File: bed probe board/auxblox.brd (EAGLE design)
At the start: 20 x 10.1 mm, 4 parts, among them CN1 3p-2.54, CN2 3p-2.54

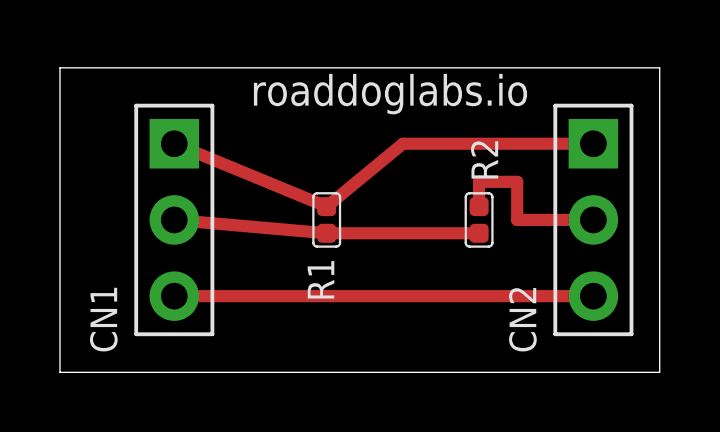
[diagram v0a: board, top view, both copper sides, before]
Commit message: update bed probe board
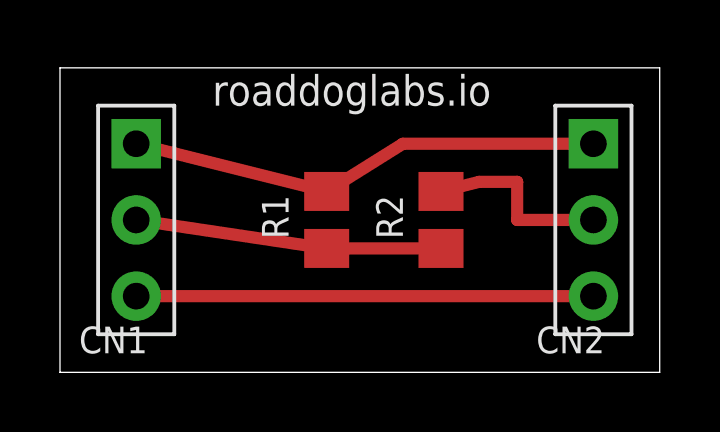
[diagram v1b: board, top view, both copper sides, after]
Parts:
- R1: value 910K 1/16W -> 1k; device Seeed-Resistor-2016:R0402 -> resistor:R0805
- R2: device Seeed-Resistor-2016:R0402 -> resistor:R0805
- moved CN1 1.27 mm to (16.5, 40.6)
- moved R2 1.27 mm to (26.7, 40.6), turned to 90 degrees
- turned R1 to 270 degrees
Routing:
- net N$1: track 14.0 -> 15.2 mm
- net N$4: track 15.1 -> 15.9 mm
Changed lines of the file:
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@@
 <?xml version="1.0" encoding="utf-8"?>
 <!DOCTYPE eagle SYSTEM "eagle.dtd">
-<eagle version="7.5.0">
+<eagle version="7.6.0">
 <drawing>
 <settings>
@@
 <wire x1="33.96" y1="45.71" x2="13.97" y2="45.71" width="0" layer="20"/>
 <wire x1="13.97" y1="45.71" x2="13.97" y2="35.56" width="0" layer="20"/>
-<text x="20.32" y="44.45" size="1.016" layer="21">roaddoglabs.io</text>
+<text x="19.05" y="44.45" size="1.016" layer="21">roaddoglabs.io</text>
 </plain>
 <attributes>
@@
 </class>
 </classes>
-<designrules name="SeeedStudio_2layer_DRU_no_angle_20140221">
-<description language="de">&lt;b&gt;EAGLE Design Rules&lt;/b&gt;
-&lt;p&gt;
-Die Standard-Design-Rules sind so gewählt, dass sie für
-die meisten Anwendungen passen. Sollte ihre Platine
-besondere Anforderungen haben, treffen Sie die erforderlichen
-Einstellungen hier und speichern die Design Rules unter
-einem neuen Namen ab.</description>
-<description language="en">&lt;b&gt;EAGLE Design Rules&lt;/b&gt;
-&lt;p&gt;
-The default Design Rules have been set to cover
-a wide range of applications. Your particular design
-may have different requirements, so please make the
-necessary adjustments and save your customized
-design rules under a new name.</description>
-<description language="zh">&lt;b&gt;Seeed Studio EAGLE Design Rules&lt;/b&gt;
-</description>
+<designrules name="dirt_cheap_dirty_boards.v1">
+<description language="en">&lt;b&gt;Dirty Cheap Dirty Board Design Rules&lt;/b&gt;
+&lt;br&gt;
+&lt;br&gt;Min width/Spacing: 5/5mil
+&lt;br&gt;Min diameter of finished hole 12mil</description>
 <param name="layerSetup" value="(1*16)"/>
 <param name="mtCopper" value="0.035mm 0.0175mm 0.035mm 0.035mm 0.035mm 0.035mm 0.035mm 0.035mm 0.035mm 0.035mm 0.035mm 0.035mm 0.035mm 0.035mm 0.0175mm 0.035mm"/>
 <param name="mtIsolate" value="1.5mm 1.1mm 0.2mm 0.15mm 0.2mm 0.15mm 0.2mm 0.15mm 0.2mm 0.15mm 0.2mm 0.15mm 0.2mm 0.15mm 0.2mm"/>
-<param name="mdWireWire" value="6mil"/>
-<param name="mdWirePad" value="6mil"/>
-<param name="mdWireVia" value="6mil"/>
-<param name="mdPadPad" value="6mil"/>
-<param name="mdPadVia" value="6mil"/>
-<param name="mdViaVia" value="6mil"/>
+<param name="mdWireWire" value="5mil"/>
+<param name="mdWirePad" value="5mil"/>
+<param name="mdWireVia" value="5mil"/>
+<param name="mdPadPad" value="5mil"/>
+<param name="mdPadVia" value="5mil"/>
+<param name="mdViaVia" value="5mil"/>
 <param name="mdSmdPad" value="0mil"/>
 <param name="mdSmdVia" value="0mil"/>
@@
 <param name="mdDrill" value="10mil"/>
 <param name="mdSmdStop" value="0mil"/>
-<param name="msWidth" value="6mil"/>
+<param name="msWidth" value="5mil"/>
 <param name="msDrill" value="12mil"/>
 <param name="msMicroVia" value="12mil"/>
@@
 <param name="mlMinCreamFrame" value="0mil"/>
 <param name="mlMaxCreamFrame" value="0mil"/>
-<param name="mlViaStopLimit" value="100mil"/>
+<param name="mlViaStopLimit" value="25mil"/>
 <param name="srRoundness" value="0"/>
 <param name="srMinRoundness" value="0mil"/>
@@
 </autorouter>
 <elements>
-<element name="R1" library="Seeed-Resistor-2016" package="R0402" value="910K 1/16W" x="22.86" y="40.64" smashed="yes">
-<attribute name="MPN" value="RC0402JR-07910KR" x="22.86" y="40.64" size="1.778" layer="27" display="off"/>
-<attribute name="NAME" x="22.225" y="39.37" size="0.889" layer="25" ratio="11" rot="R270"/>
+<element name="R1" library="resistor" package="R0805" value="1k" x="22.86" y="40.64" smashed="yes" rot="R270">
+<attribute name="NAME" x="21.59" y="40.005" size="0.889" layer="25" ratio="11" rot="R90"/>
 </element>
-<element name="R2" library="Seeed-Resistor-2016" package="R0402" value="3.3K" x="27.94" y="40.64" smashed="yes" rot="R180">
-<attribute name="MPN" value="RC0402JR-073K3L" x="27.94" y="40.64" size="1.778" layer="27" rot="R180" display="off"/>
-<attribute name="NAME" x="28.575" y="41.91" size="0.889" layer="25" ratio="11" rot="R90"/>
+<element name="R2" library="resistor" package="R0805" value="3.3K" x="26.67" y="40.64" smashed="yes" rot="R90">
+<attribute name="NAME" x="25.4" y="40.005" size="0.889" layer="25" ratio="11" rot="R90"/>
 </element>
-<element name="CN1" library="Seeed-Connector -2016" package="H3-2.54" value="3p-2.54" x="17.78" y="40.64" smashed="yes">
-<attribute name="NAME" x="15.875" y="36.195" size="0.889" layer="25" ratio="11" rot="R90"/>
+<element name="CN1" library="Seeed-Connector -2016" package="H3-2.54" value="3p-2.54" x="16.51" y="40.64" smashed="yes">
+<attribute name="NAME" x="14.605" y="36.195" size="0.889" layer="25" ratio="11"/>
 </element>
 <element name="CN2" library="Seeed-Connector -2016" package="H3-2.54" value="3p-2.54" x="31.75" y="40.64" smashed="yes">
-<attribute name="NAME" x="29.845" y="36.195" size="0.889" layer="25" ratio="11" rot="R90"/>
+<attribute name="NAME" x="29.845" y="36.195" size="0.889" layer="25" ratio="11"/>
 </element>
 </elements>
@@
 <contactref element="CN2" pad="3"/>
 <contactref element="CN1" pad="3"/>
-<wire x1="17.78" y1="38.1" x2="31.75" y2="38.1" width="0.4064" layer="1"/>
+<wire x1="16.51" y1="38.1" x2="31.75" y2="38.1" width="0.4064" layer="1"/>
 </signal>
 <signal name="N$4">
@@
 <contactref element="CN1" pad="1"/>
 <contactref element="R1" pad="1"/>
-<wire x1="17.78" y1="43.18" x2="22.86" y2="41.0845" width="0.4064" layer="1"/>
-<wire x1="22.86" y1="41.0845" x2="25.4" y2="43.18" width="0.4064" layer="1"/>
+<wire x1="16.51" y1="43.18" x2="22.86" y2="41.59" width="0.4064" layer="1"/>
+<wire x1="22.86" y1="41.59" x2="25.4" y2="43.18" width="0.4064" layer="1"/>
 <wire x1="25.4" y1="43.18" x2="31.75" y2="43.18" width="0.4064" layer="1"/>
 </signal>
@@
 <wire x1="29.21" y1="40.64" x2="29.21" y2="41.91" width="0.4064" layer="1"/>
 <wire x1="29.21" y1="41.91" x2="27.94" y2="41.91" width="0.4064" layer="1"/>
-<wire x1="27.94" y1="41.91" x2="27.94" y2="41.0845" width="0.4064" layer="1"/>
+<wire x1="27.94" y1="41.91" x2="26.67" y2="41.59" width="0.4064" layer="1"/>
 </signal>
 <signal name="N$5">
@@
 <contactref element="R2" pad="1"/>
 <contactref element="R1" pad="2"/>
-<wire x1="17.78" y1="40.64" x2="22.86" y2="40.1955" width="0.4064" layer="1"/>
-<wire x1="22.86" y1="40.1955" x2="27.94" y2="40.1955" width="0.4064" layer="1"/>
+<wire x1="16.51" y1="40.64" x2="22.86" y2="39.69" width="0.4064" layer="1"/>
+<wire x1="22.86" y1="39.69" x2="26.67" y2="39.69" width="0.4064" layer="1"/>
 </signal>
 </signals>
